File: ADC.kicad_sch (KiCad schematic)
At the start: 6 parts, among them IC301 TLA2518IRTER, J301 ADC AFE IN

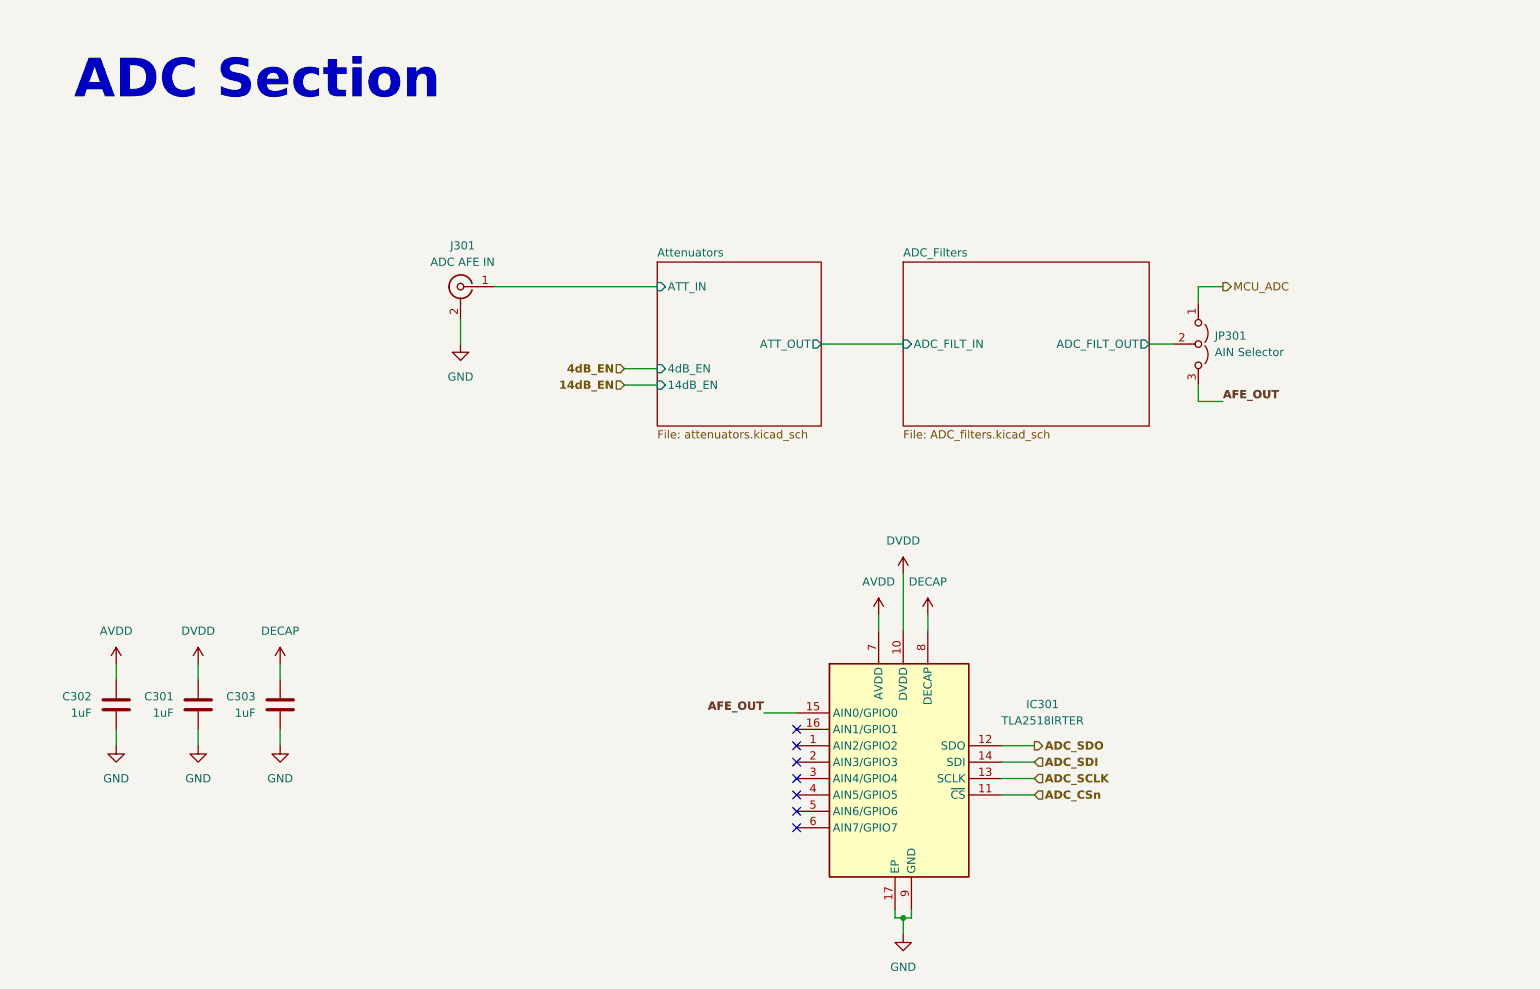
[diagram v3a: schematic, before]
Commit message: finished individual block placement and started integrating, might need to change the AFEs length
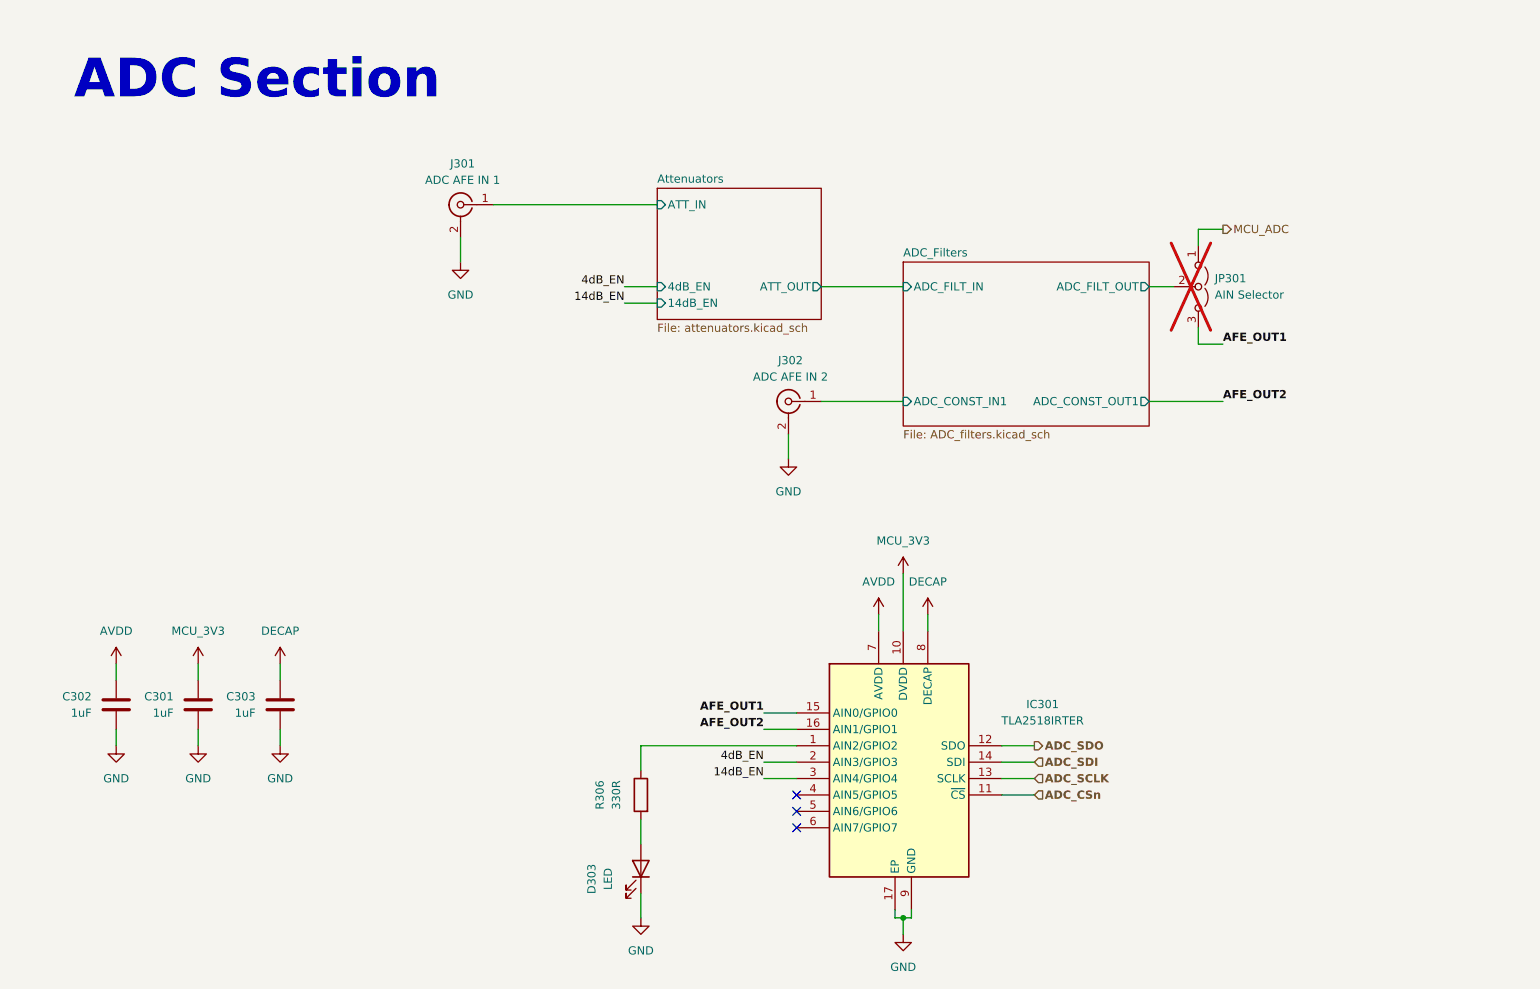
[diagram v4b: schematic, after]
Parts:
- added D303: LED, LED_SMD:LED_0805_2012Metric, symbol Device:LED
- added J302: ADC AFE IN 2, DOSIN-801-0083:CONN4_DOSIN-801_DOS, symbol Connector:Conn_Coaxial
- added R306: 330R, Resistor_SMD:R_0603_1608Metric, symbol Device:R
- C301, C302, C303: footprint (none) -> Capacitor_SMD:C_0603_1608Metric; MPN (none) -> 0603X105K250CT
- IC301: footprint QFN50P300X300X80-17N-D -> TLA2518IRTER:QFN50P300X300X80-17N-D; MPN (none) -> TLA2518IRTER
- J301: value ADC AFE IN -> ADC AFE IN 1; footprint (none) -> DOSIN-801-0083:CONN4_DOSIN-801_DOS; MPN (none) -> DOSIN-801-0083
- JP301: footprint (none) -> Jumper:SolderJumper-3_P1.3mm_Open_Pad1.0x1.5mm; now not fitted
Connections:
- net 14dB_EN: now also IC301.3 (AIN4/GPIO4)
- net 4dB_EN: now also IC301.2 (AIN3/GPIO3)
- net GND: now also D303.1 (K), J302.2 (Ext)
- net at IC301.1 (AIN2/GPIO2): now also R306.1
- net AFE_OUT2: now reaches IC301.16 (AIN1/GPIO1)
- net AFE_OUT renamed AFE_OUT1
- net DVDD renamed MCU_3V3
- new net: D303.2 (A), R306.2
- new net ADC_Filters/ADC_CONST_IN1: J302.1 (In)
- no-connect marks 7 -> 3
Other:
- sheet ADC_Filters ports: added ADC_CONST_IN1, ADC_CONST_OUT1; removed none
- moved on the sheet: J301
